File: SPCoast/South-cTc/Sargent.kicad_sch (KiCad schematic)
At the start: 1 part

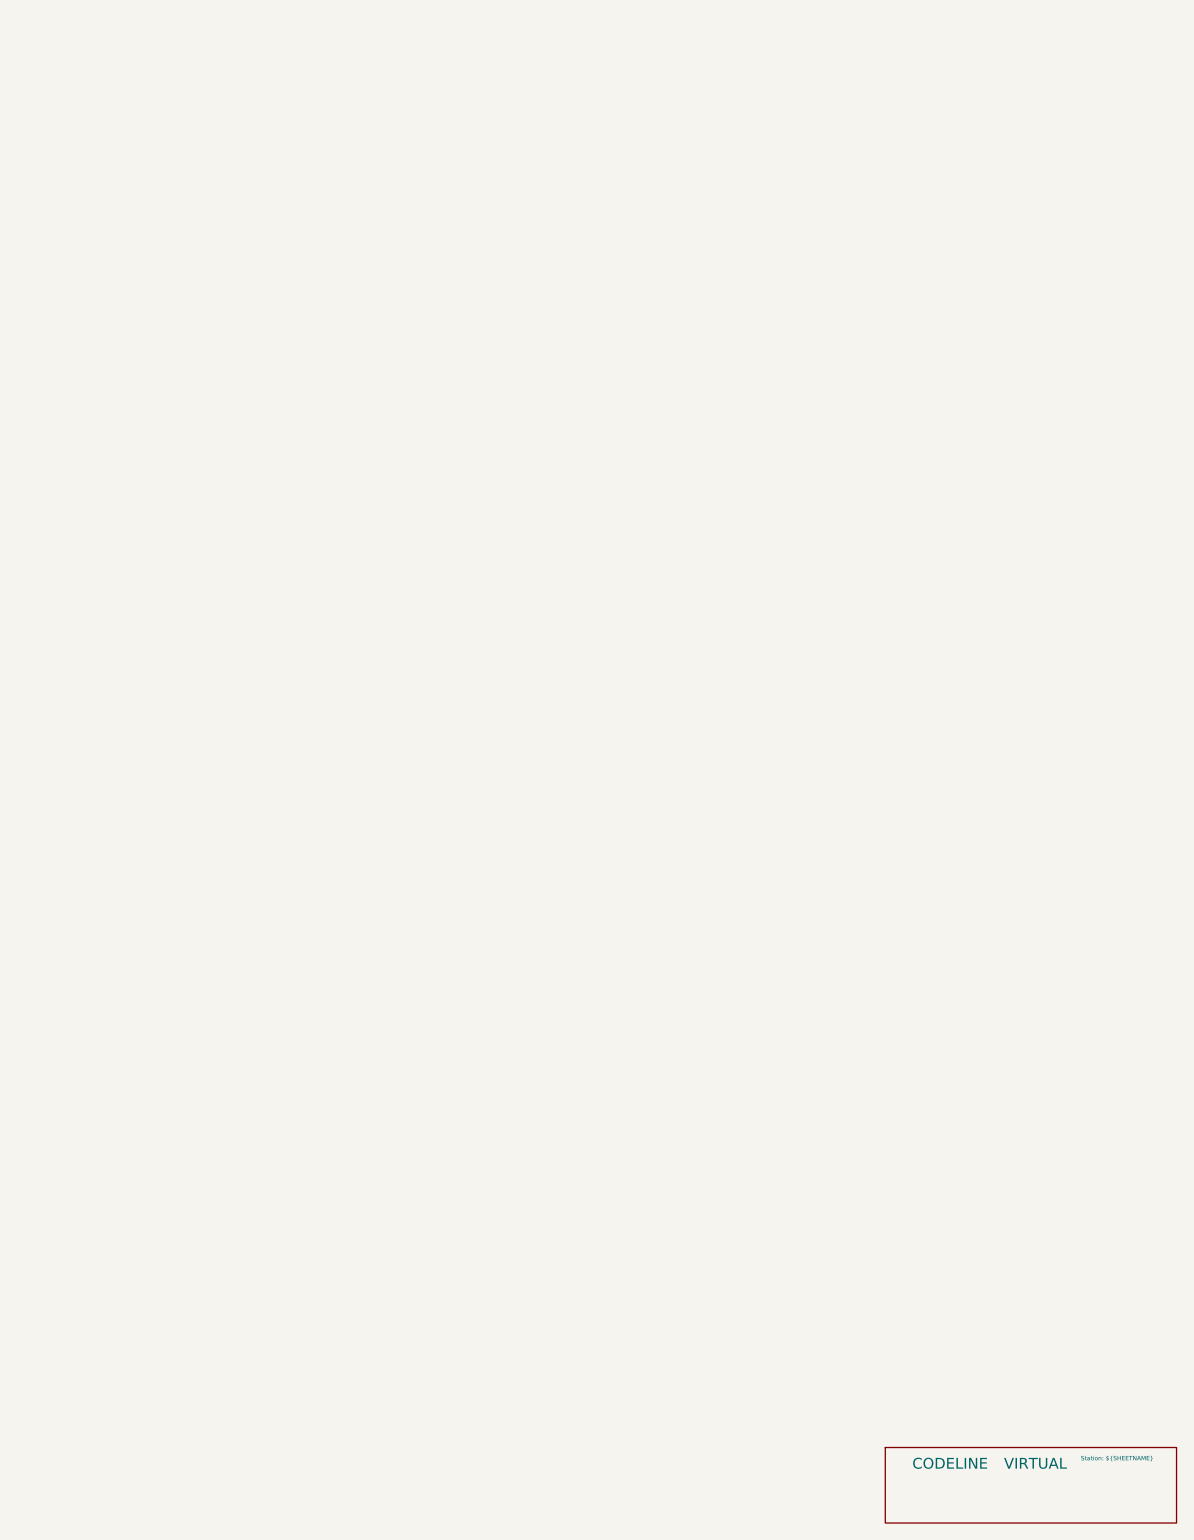
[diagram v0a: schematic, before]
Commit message: SPCoast: derail pin R, track circuit names end in T, code line symbols on the root sheet
Working-tree changes from the 2026-10-01..03 vocabulary review with
FieldUnit-Subdivision (docs/adr/0001-code-line-type-contract.md):

- Switch_Powered_Derail pin 2 is R (through path = REVERSE) in the seven
  plant schematics (library Railroad.kicad_sym renamed alongside; not in git)
- Luchessa track circuits renamed to end in T (1SAT, 2NAAT, ...); MC1 moved
  to CP Gilroy's house
- South-cTc: transports (MQTT, TimeCode, CMRInet, Loconet) on the root
  sheet on the CtcMachine Transports pin; field stations as encoding
  instances on the Luchessa sheet; two Luchessa lamp tokens renamed
- Six plant projects (Christopher, Corporal, GilroyCalTrain,
  GilroyInterchange, Sargent, Watsonville) added as drawn so far; Watsonville
  updated 2026-10-02

Co-Authored-By: Claude Fable 5.1 <noreply@anthropic.com>
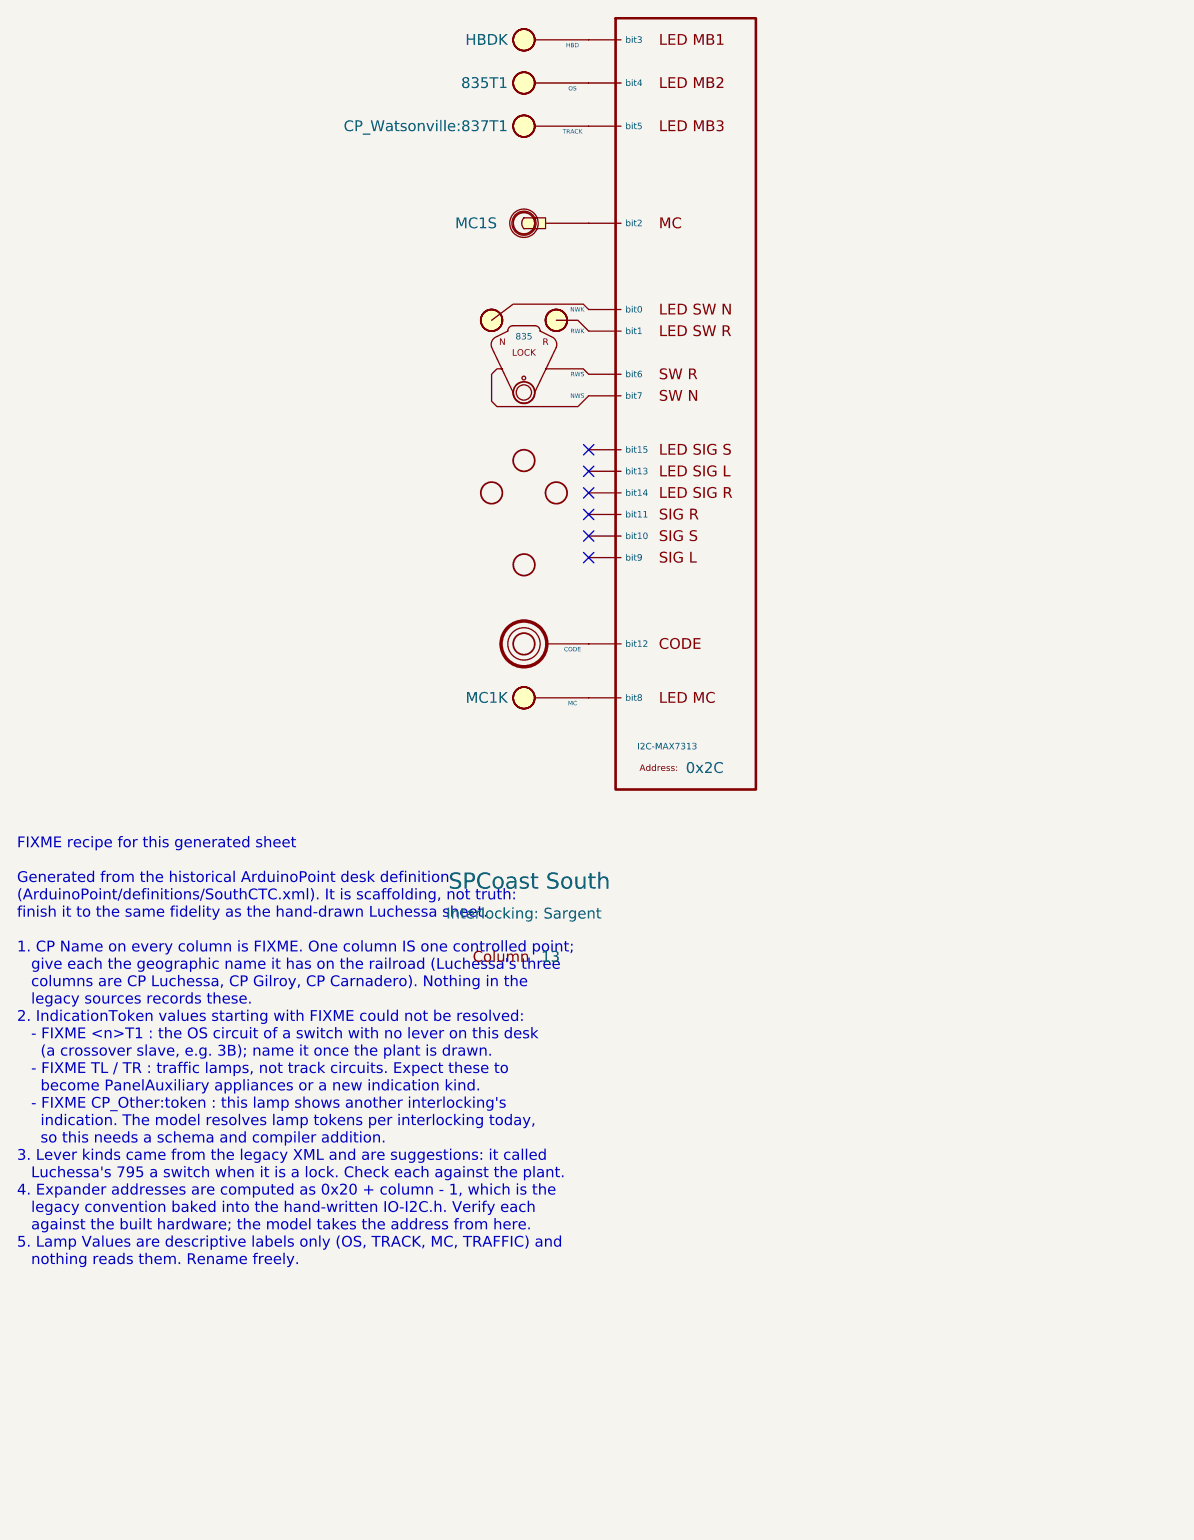
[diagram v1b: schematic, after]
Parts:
- removed CODELINE6: VIRTUAL, symbol RailroadPanel:Codeline-Virtual
- added CDE13: CODE, symbol RailroadPanel:PanelCode
- added COL33: 13, symbol RailroadPanel:PanelColumn
- added LKL13: 835, symbol RailroadPanel:PanelLock
- added LMP131: HBD, symbol RailroadPanel:PanelLamp-RED
- added LMP132: OS, symbol RailroadPanel:PanelLamp-RED
- added LMP133: TRACK, symbol RailroadPanel:PanelLamp-RED
- added MCK13: MC, symbol RailroadPanel:PanelLamp-YELLOW
- added MCL13: MC1, symbol RailroadPanel:PanelMCall
- added U33: 0x2C, symbol RailroadPanel:PanelColumn-MAX7313
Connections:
- new net: COL33.8 (Column), MCK13.1 (Column)
- new net: MCK13.2 (LAMP), U33.9 (bit8)
- new net: LKL13.5 (NWK), U33.1 (bit0)
- new net: CDE13.2 (CODE), U33.13 (bit12)
- new net: LKL13.4 (RWK), U33.2 (bit1)
- new net: MCL13.2 (SW), U33.3 (bit2)
- new net: LMP131.2 (LAMP), U33.4 (bit3)
- new net: LMP132.2 (LAMP), U33.5 (bit4)
- new net: LMP133.2 (LAMP), U33.6 (bit5)
- new net: LKL13.3 (RWS), U33.7 (bit6)
- new net: LKL13.2 (NWS), U33.8 (bit7)
- new net: COL33.3 (Column), LMP133.1 (Column)
- new net: COL33.2 (Column), LMP132.1 (Column)
- new net: CDE13.1 (Column), COL33.7 (Column)
- new net: COL33.4 (Column), MCL13.1 (Column)
- new net: COL33.1 (Column), LMP131.1 (Column)
- new net: COL33.5 (Column), LKL13.1 (Column)
- no-connect marks 0 -> 6
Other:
- note added: "FIXME recipe for this generated sheet Generated from the historical ArduinoPoint desk definition (ArduinoPoint/definitions/SouthCTC.xml). It is scaffolding, not truth: finish it to the same fidelity as the hand-drawn Luchessa sheet. 1. CP Name on every column is FIXME. One column IS one controlled point; give each the geographic name it has on the railroad (Luchessa's three columns are CP Luchess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"

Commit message: SPCoast: Address field and Kind on PanelColumn-MAX7313; encoding Values; HBA; Watsonville update
Owner's drawing changes of 2026-10-02..03 (FieldUnit-Subdivision ADR 0002 D18
and the owner's responses):

- PanelColumn-MAX7313: the expander address moves from the Value to an
  Address field (Value is ${Address}); BusKind renamed Kind (I2C-MAX7313)
- Luchessa encoding symbols: Value "US&S 506 time-coded DC pulses"
- Sargent: HBD renamed HBA; traffic indications [NSEW]FLK
- Watsonville schematic brought to a usable state
- Luchessa plant: track circuits end in T; MC1 at CP Gilroy's house

Co-Authored-By: Claude Fable 5.1 <noreply@anthropic.com>
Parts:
- LMP131: IndicationToken HBDK -> HBAK
- U33: Address (none) -> 0x2C; BusKind I2C-MAX7313 -> (none); Kind (none) -> I2C-MAX7313
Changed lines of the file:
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@@
 		(property "Value" "0x2C"
 			(at 99.06 112.395 0)
+			(hide yes)
 			(show_name no)
 			(do_not_autoplace yes)
@@
 			)
 		)
-		(property "BusKind" "I2C-MAX7313"
+		(property "Role" "IODRIVER"
+			(at 97.79 107.315 0)
+			(hide yes)
+			(show_name no)
+			(do_not_autoplace no)
+			(effects
+				(font
+					(size 1.27 1.27)
+				)
+			)
+		)
+		(property "Kind" "I2C-MAX7313"
 			(at 93.345 109.855 0)
 			(show_name no)
-			(do_not_autoplace yes)
+			(do_not_autoplace no)
 			(effects
 				(font
@@
 			)
 		)
-		(property "Role" "IODRIVER"
-			(at 99.06 72.39 0)
-			(hide yes)
+		(property "Address" "0x2C"
+			(at 101.346 112.268 0)
 			(show_name no)
 			(do_not_autoplace no)
@@
 			)
 		)
-		(property "IndicationToken" "HBDK"
+		(property "IndicationToken" "HBAK"
 			(at 78.105 26.67 0)
 			(show_name no)

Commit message: SPCoast: owner's edits: schematics synced with the revised symbol libraries (baseline)
Update Symbols from Library on all plant and desk sheets; CP values for
Christopher, GilroyInterchange and Luchessa; Restricted Speed markers
consolidated in Corporal, Luchessa and Sargent.

Observed in the diff, not changed by the sweep that follows: CP changed on 23
symbols (Christopher: prefix removed, 815/815A/IND now Christopher North) and
added on 12 (GilroyInterchange); two lamps' Color reset to their symbol variant
(Christopher LMP93 red -> yellow, Sargent LMP133 yellow -> red).

Verified: netlists keep their net counts (Christopher 33, Corporal 26,
GilroyCalTrain 27, GilroyInterchange 22, Luchessa 34, Sargent 18, Watsonville
96, South-cTc 341); desk compiles to 75 appliances, 137 bindings, 14 columns;
no root-UUID regression.

Co-Authored-By: Claude Sonnet 5.5 <noreply@anthropic.com>
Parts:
- LMP133: Color yellow -> red
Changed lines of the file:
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@@
 			)
 		)
-		(property "Description" "One physical desk lamp. Value is a free descriptive label (e.g. OS, TRACK, MC) and is not used elsewhere. IndicationToken is a comma-separated list of indication names (track circuits such as 795T1,2NAA,799T1, or tokens such as MC1K) OR'd to drive this one lamp. All listed indications are still individually on the CodeLine wire"
+		(property "Description" "One physical model board lamp. Value is a free descriptive label (e.g. OS, TRACK, MC) and is not used elsewhere. IndicationToken is a comma-separated list of indication names (track circuits such as 795T1,2NAA,799T1, or tokens such as MC1K) OR'd to drive this one lamp. All listed indications are still individually on the CodeLine wire"
 			(at 80.01 111.76 0)
 			(hide yes)
@@
 			)
 		)
-		(property "Description" "One physical desk lamp. Value is a free descriptive label (e.g. OS, TRACK, MC) and is not used elsewhere. IndicationToken is a comma-separated list of indication names (track circuits such as 795T1,2NAA,799T1, or tokens such as MC1K) OR'd to drive this one lamp. All listed indications are still individually on the CodeLine wire"
+		(property "Description" "One physical model board lamp. Value is a free descriptive label (e.g. OS, TRACK, MC) and is not used elsewhere. IndicationToken is a comma-separated list of indication names (track circuits such as 795T1,2NAA,799T1, or tokens such as MC1K) OR'd to drive this one lamp. All listed indications are still individually on the CodeLine wire"
 			(at 79.375 46.355 0)
 			(hide yes)
@@
 			)
 		)
-		(property "Color" "yellow"
+		(property "Color" "red"
 			(at 79.375 45.085 0)
 			(hide yes)
@@
 			)
 		)
-		(property "Description" "One physical desk lamp. Value is a free descriptive label (e.g. OS, TRACK, MC) and is not used elsewhere. IndicationToken is a comma-separated list of indication names (track circuits such as 795T1,2NAA,799T1, or tokens such as MC1K) OR'd to drive this one lamp. All listed indications are still individually on the CodeLine wire"
+		(property "Description" "One physical model board lamp. Value is a free descriptive label (e.g. OS, TRACK, MC) and is not used elsewhere. IndicationToken is a comma-separated list of indication names (track circuits such as 795T1,2NAA,799T1, or tokens such as MC1K) OR'd to drive this one lamp. All listed indications are still individually on the CodeLine wire"
 			(at 79.375 41.275 0)
 			(hide yes)
@@
 			)
 		)
-		(property "Description" "Generic 1-bit dispatcher-facing appliance (Maintainer Call, switch heater, bungalow door, etc).  ControlToken must be declared explicitly."
+		(property "Description" "Maintainer Call Lever"
 			(at 80.01 55.245 0)
 			(hide yes)
@@
 			)
 		)
-		(property "Description" "One physical desk lamp. Value is a free descriptive label (e.g. OS, TRACK, MC) and is not used elsewhere. IndicationToken is a comma-separated list of indication names (track circuits such as 795T1,2NAA,799T1, or tokens such as MC1K) OR'd to drive this one lamp. All listed indications are still individually on the CodeLine wire"
+		(property "Description" "One physical model board lamp. Value is a free descriptive label (e.g. OS, TRACK, MC) and is not used elsewhere. IndicationToken is a comma-separated list of indication names (track circuits such as 795T1,2NAA,799T1, or tokens such as MC1K) OR'd to drive this one lamp. All listed indications are still individually on the CodeLine wire"
 			(at 79.375 36.195 0)
 			(hide yes)

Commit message: SPCoast: owner's edits: NextCP names, Christopher heads and masts, Sargent milepost, Watsonville circuits and desk tokens (baseline)
- NextCP values name interlockings: GilroyCalTrain CP2 -> Gilroy Interchange;
  Luchessa CP1 -> Gilroy Interchange, CP2 -> Hollister, CP3 and CP4 ->
  Christopher.
- Christopher: the two unnamed dwarf masts, their IRJ-Signals (now plain IRJs)
  and heads removed; remaining heads lettered A, B, C.
- Sargent MAIN HOUSE Milepost 83.5.
- Watsonville circuits SDT -> 0DT and SAT -> 0AT; desk tokens 0DT, 0AT, AT and
  Watsonville:837T1 follow.

Verified: netlists rebuild (Christopher 30, Corporal 27, GilroyCalTrain 28,
GilroyInterchange 23, Luchessa 35, Sargent 19, Watsonville 97, South-cTc 341);
Christopher has no mast or head diagnostics left; desk compiles to 75
appliances, 137 bindings, 14 columns; no root-UUID regression.

Co-Authored-By: Claude Sonnet 5.5 <noreply@anthropic.com>
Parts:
- LMP133: IndicationToken CP_Watsonville:837T1 -> Watsonville:837T1
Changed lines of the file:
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@@
 			)
 		)
-		(property "IndicationToken" "CP_Watsonville:837T1"
+		(property "IndicationToken" "Watsonville:837T1"
 			(at 78.105 36.83 0)
 			(show_name no)

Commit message: SPCoast: owner's edits: Watsonville virtual indications 0100T and 0101T, circuits 01T..03T, desk tokens (baseline)
Includes typos in the member lists (a period for a comma, a missing 25T1, a stray 03T), corrected in the next commit.

Co-Authored-By: Claude Sonnet 5.5 <noreply@anthropic.com>
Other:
- note removed: "FIXME recipe for this generated sheet Generated from the historical ArduinoPoint desk definition (ArduinoPoint/definitions/SouthCTC.xml). It is scaffolding, not truth: finish it to the same fidelity as the hand-drawn Luchessa sheet. 1. CP Name on every column is FIXME. One column IS one controlled point; give each the geographic name it has on the railroad (Luchessa's three columns are CP Luchess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"
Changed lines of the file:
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@@
 		(comment 1 "JPlocher")
-	)
-	(text "FIXME recipe for this generated sheet\n\nGenerated from the historical ArduinoPoint desk definition\n(ArduinoPoint/definitions/SouthCTC.xml). It is scaffolding, not truth:\nfinish it to the same fidelity as the hand-drawn Luchessa sheet.\n\n1. CP Name on every column is FIXME. One column IS one controlled point;\n   give each the geographic name it has on the railroad (Luchessa's three\n   columns are CP Luchessa, CP Gilroy, CP Carnadero). Nothing in the\n   legacy sources records these.\n2. IndicationToken values starting with FIXME could not be resolved:\n   - FIXME <n>T1 : the OS circuit of a switch with no lever on this desk\n     (a crossover slave, e.g. 3B); name it once the plant is drawn.\n   - FIXME TL / TR : traffic lamps, not track circuits. Expect these to\n     become PanelAuxiliary appliances or a new indication kind.\n   - FIXME CP_Other:token : this lamp shows another interlocking's\n     indication. The model resolves lamp tokens per interlocking today,\n     so this needs a schema and compiler addition.\n3. Lever kinds came from the legacy XML and are suggestions: it called\n   Luchessa's 795 a switch when it is a lock. Check each against the plant.\n4. Expander addresses are computed as 0x20 + column - 1, which is the\n   legacy convention baked into the hand-written IO-I2C.h. Verify each\n   against the built hardware; the model takes the address from here.\n5. Lamp Values are descriptive labels only (OS, TRACK, MC, TRAFFIC) and\n   nothing reads them. Rename freely.\n"
-		(exclude_from_sim no)
-		(at 20.32 120.65 0)
-		(effects
-			(font
-				(size 1.27 1.27)
-			)
-			(justify left top)
-		)
 	)
 	(no_connect

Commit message: chore(kicad): refresh instances to the ADR 0003 libraries (InterlockingPlant 95f53e2)
- Desk sheets (South-cTc/*) and the Sargent sandbox: embedded PanelSwitch, PanelLock,
  PanelSignal, PanelMCall, PanelCode, PanelLamp-*, PanelColumn-MAX7313 definitions refreshed
  from the library (refresh_embedded.py, checked against the pre-pass library: only Description
  text had drifted). Instance Role APPLIANCE -> PANEL (77).
- Plant sheets: powered-switch instance Kind SWITCH_POWERED -> SWITCH_REMOTE (21), matching the
  library (sweep_role_kind_fields.py).

Verified:
- verify_symbol_diff.py: same symbols, lib_ids and positions; only Role/Kind changed.
- Nets unchanged: Christopher 30, Corporal 27, GilroyCalTrain 28, GilroyInterchange 23,
  Luchessa 35, Sargent 61, Watsonville 99, South-cTc 341.
- parse_kicad_plant.py --format text identical before/after for all seven plants.
- Desk compile 75/137/14, diagnostics identical; the 7 desk locks bind WLS/~{WLS}/~{WLK}/WLK
  to the bits that were NWS/RWS/RWK/NWK.
- No sheet or project outside Luchessa carries the copied root UUID.

Co-Authored-By: Claude Opus 5.5 <noreply@anthropic.com>
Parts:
- CDE13, LKL13, LMP131, LMP132, LMP133, MCK13, MCL13: Role APPLIANCE -> PANEL
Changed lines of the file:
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@@
 			)
 		)
-		(property "Role" "APPLIANCE"
+		(property "Role" "PANEL"
 			(at 80.01 101.6 0)
 			(hide yes)
@@
 			)
 		)
-		(property "Role" "APPLIANCE"
+		(property "Role" "PANEL"
 			(at 80.01 39.37 0)
 			(hide yes)
@@
 			)
 		)
-		(property "Role" "APPLIANCE"
+		(property "Role" "PANEL"
 			(at 80.01 34.29 0)
 			(hide yes)
@@
 			)
 		)
-		(property "Role" "APPLIANCE"
+		(property "Role" "PANEL"
 			(at 80.01 90.17 0)
 			(hide yes)
@@
 			)
 		)
-		(property "Role" "APPLIANCE"
+		(property "Role" "PANEL"
 			(at 86.36 44.45 0)
 			(hide yes)
@@
 			)
 		)
-		(property "Role" "APPLIANCE"
+		(property "Role" "PANEL"
 			(at 80.01 29.21 0)
 			(hide yes)
@@
 			)
 		)
-		(property "Role" "APPLIANCE"
+		(property "Role" "PANEL"
 			(at 80.645 74.93 0)
 			(hide yes)
